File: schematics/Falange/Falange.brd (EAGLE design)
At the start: 78.7 x 63.8 mm, 44 parts, among them IC1 7909, IC2 7809, IC3 TL082P

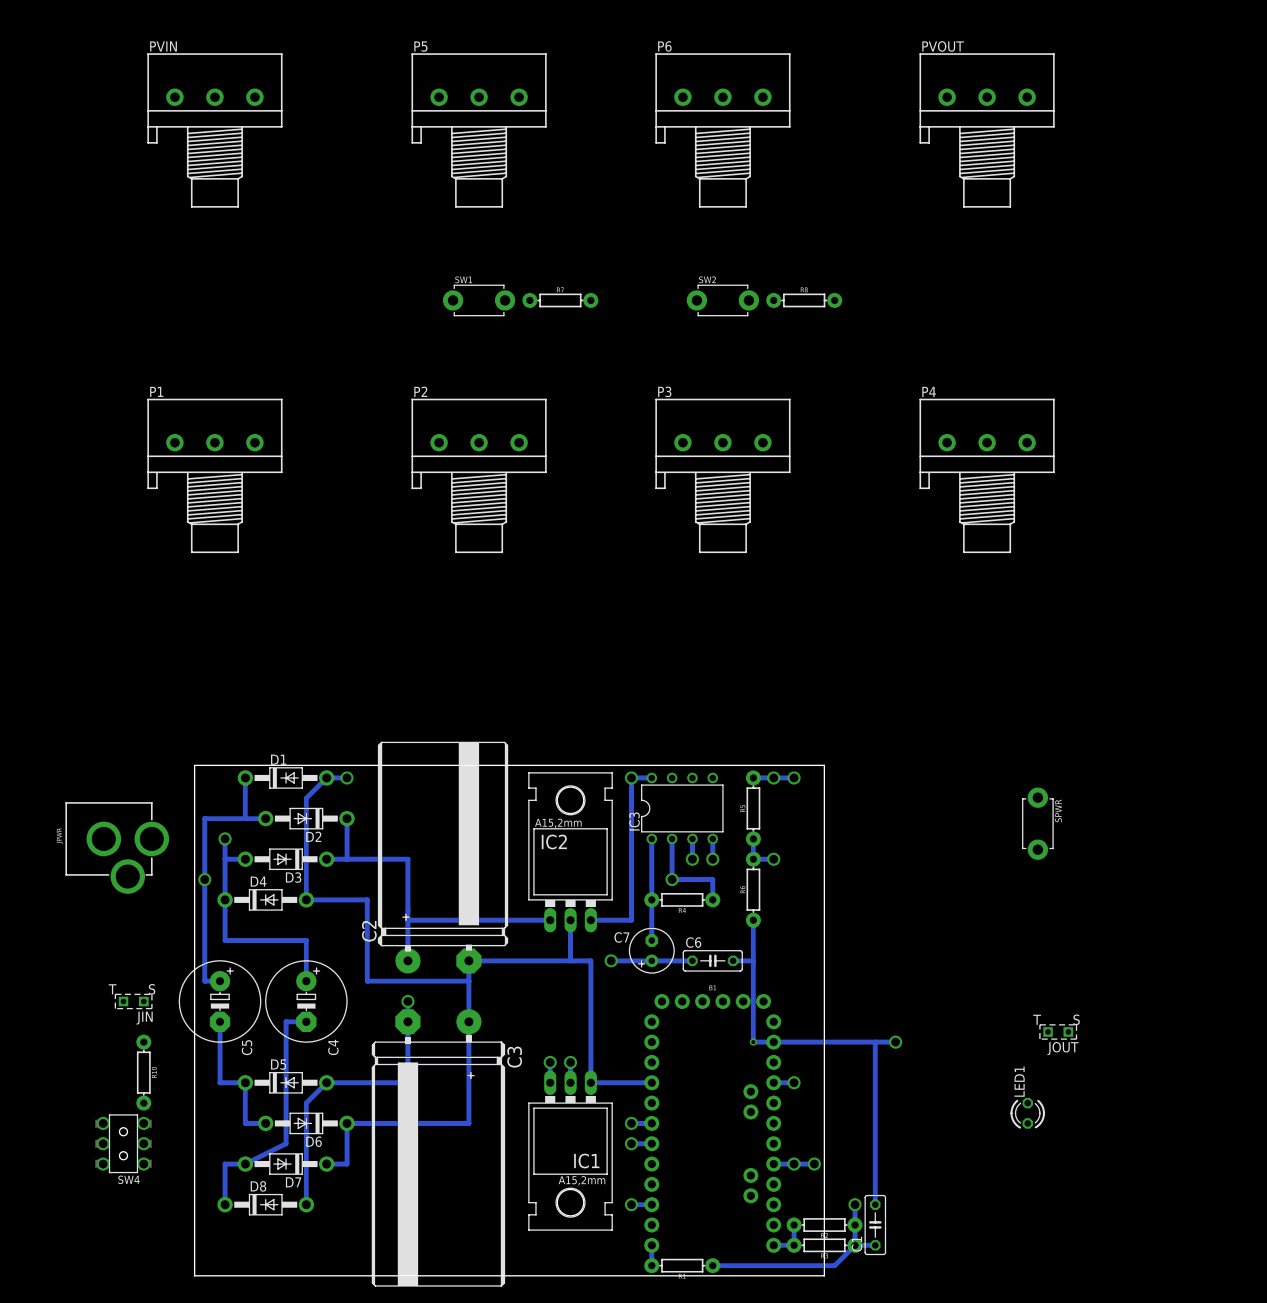
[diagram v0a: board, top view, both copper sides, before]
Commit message: update falange schematics
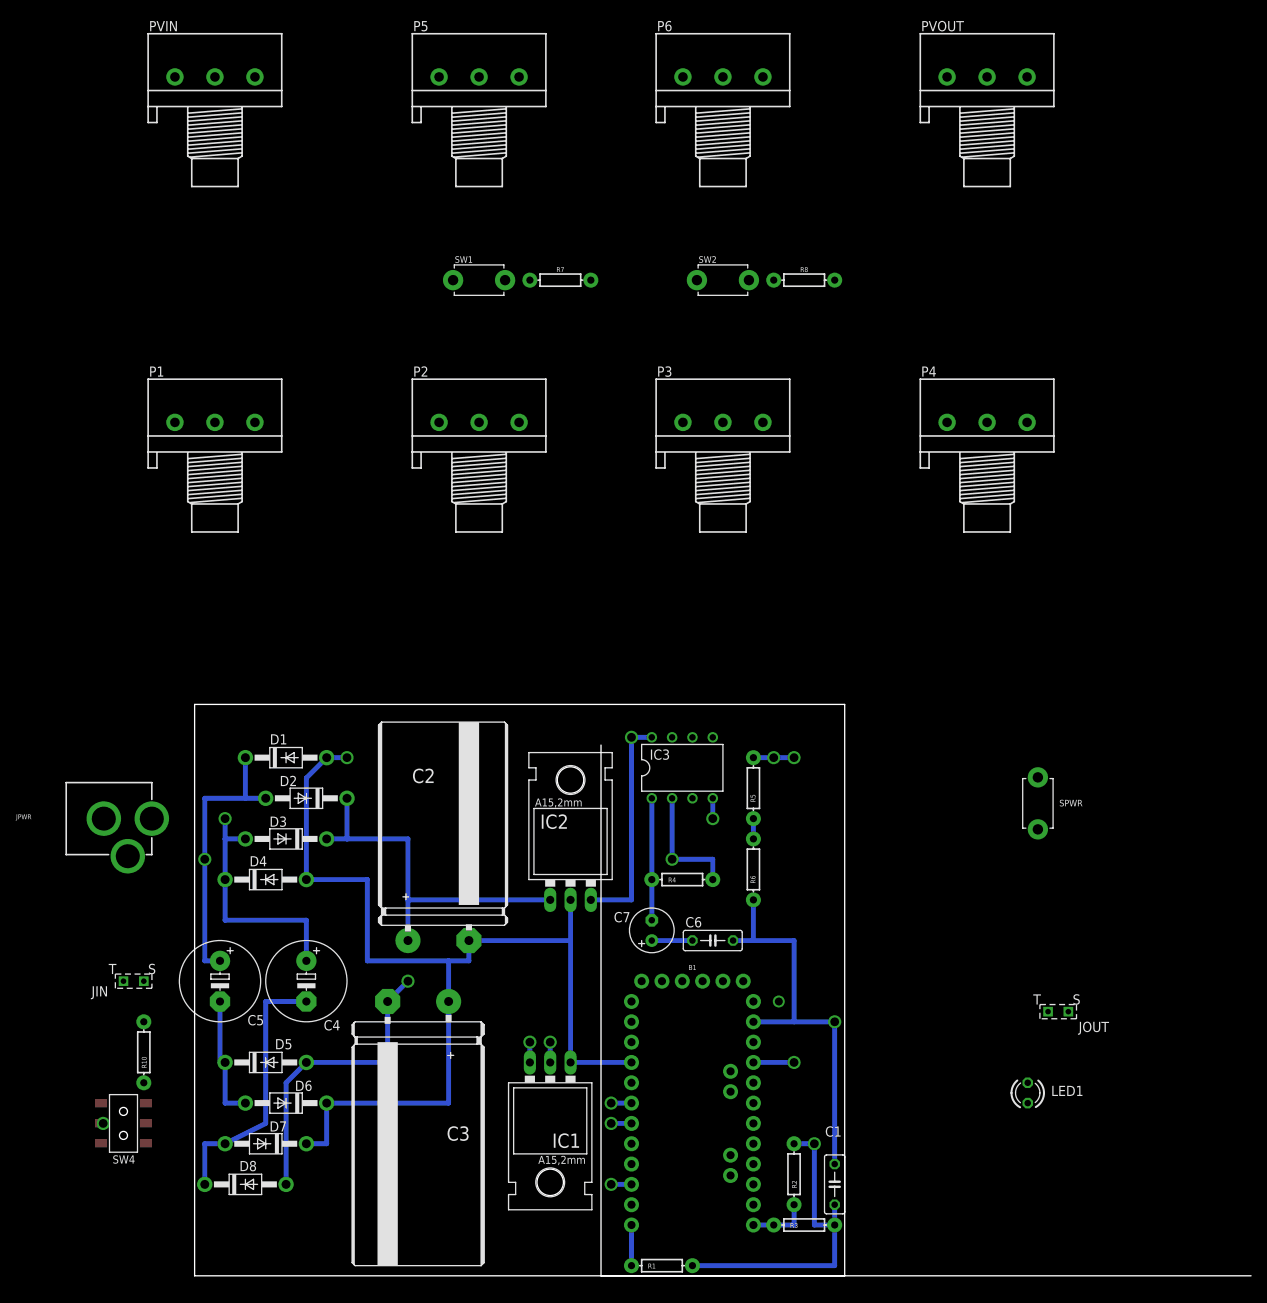
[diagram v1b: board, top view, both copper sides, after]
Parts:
- moved R2 7.41 mm to (74.9, 12.7), turned to 270 degrees
- moved C1 7.18 mm to (80.0, 11.4)
- moved IC3 5.08 mm to (61.0, 63.5)
- moved D5 3.59 mm to (8.89, 26.7)
- moved C3 3.59 mm to (27.9, 17.8)
- moved D6 3.59 mm to (11.4, 21.6)
- moved D7 3.59 mm to (8.89, 16.5)
- moved D8 3.59 mm to (6.35, 11.4)
- moved B1 3.59 mm to (62.2, 21.6)
- moved IC1 3.59 mm to (44.5, 22.9)
- moved R3 3.59 mm to (76.2, 6.35)
- moved P5 2.54 mm to (35.6, 149.9)
- moved P6 2.54 mm to (66.0, 149.9)
- moved PVIN 2.54 mm to (2.54, 149.9)
- moved PVOUT 2.54 mm to (99.1, 149.9)
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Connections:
- net N$1 renamed PWRTIP
- net N$3 renamed PWRSLV
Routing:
- net IN: track 165.6 -> 2.54 mm, vias 4 -> 0
- net N$15: track 119.3 -> 0.00 mm, vias 2 -> 0
- net N$32: track 82.4 -> 5.08 mm, vias 2 -> 0
- net JP1: track 237.6 -> 292.1 mm
- net +5V: track 355.2 -> 371.3 mm
- net JP8-2: track 238.1 -> 253.8 mm
- net N$11: track 12.0 -> 0.00 mm, vias 2 -> 0
- net -9V: track 44.3 -> 48.8 mm
- net JL1: track 94.4 -> 98.8 mm
- net JS1: track 317.2 -> 313.1 mm
- net N$9: track 139.4 -> 141.9 mm
- net JP2: track 179.4 -> 182.0 mm
- net MZ2: track 5.08 -> 7.62 mm
- net N$6: track 41.9 -> 44.5 mm, vias 0 -> 1
- net N$2: track 18.4 -> 15.9 mm
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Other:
- board size 78.7 x 63.8 mm -> 132.1 x 71.4 mm
- board text added: "1"
- board text added: "10"
- board text added: "2"
- board text added: "20"
- board text added: "25 holes (vertical)"
- board text added: "3"
- board text added: "30"
- board text added: "32 holes (horizontal)"
- board text added: "4"
- board text added: "5"
- board text added: "6"
- board text added: "7"
- board text added: "8"
- board text added: "9"
- board text added: "A"
- board text added: "B"
- board text added: "C"
- board text added: "D"
- board text added: "E"
- board text added: "F"
- board text added: "G"
- board text added: "H"
- board text added: "I"
- board text added: "J"
- board text added: "K"
- board text added: "L"
- board text added: "M"
- board text added: "N"
- board text added: "O"
- board text added: "P"
- board text added: "Q"
- board text added: "R"
- board text added: "S"
- board text added: "T"
- board text added: "U"
- board text added: "V"
- board text added: "W"
- board text added: "X"
- board text added: "Y"
- board text added: "Z"
- board text added: "a"
- board text added: "b"
